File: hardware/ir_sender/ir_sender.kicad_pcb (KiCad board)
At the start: 2 copper layers, 3 parts, among them J1 Conn_01x05

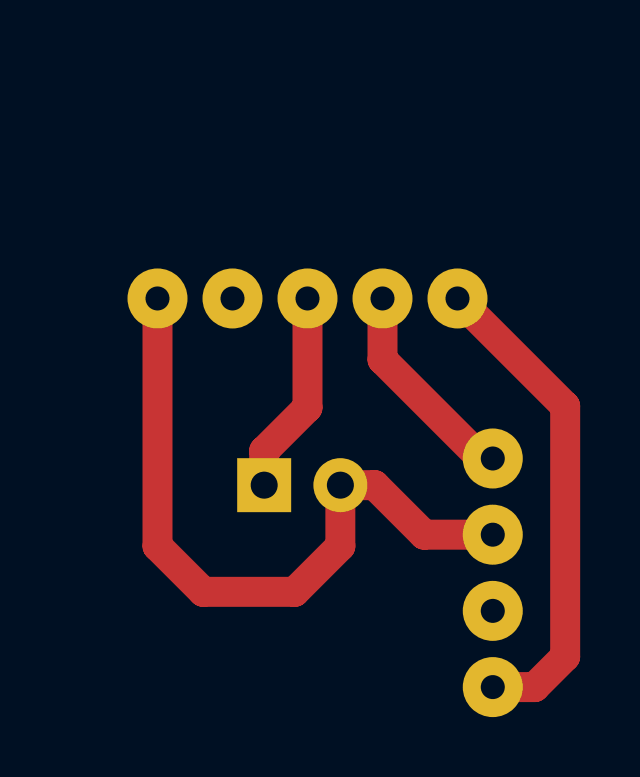
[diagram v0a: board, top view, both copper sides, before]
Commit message: New ir sender board
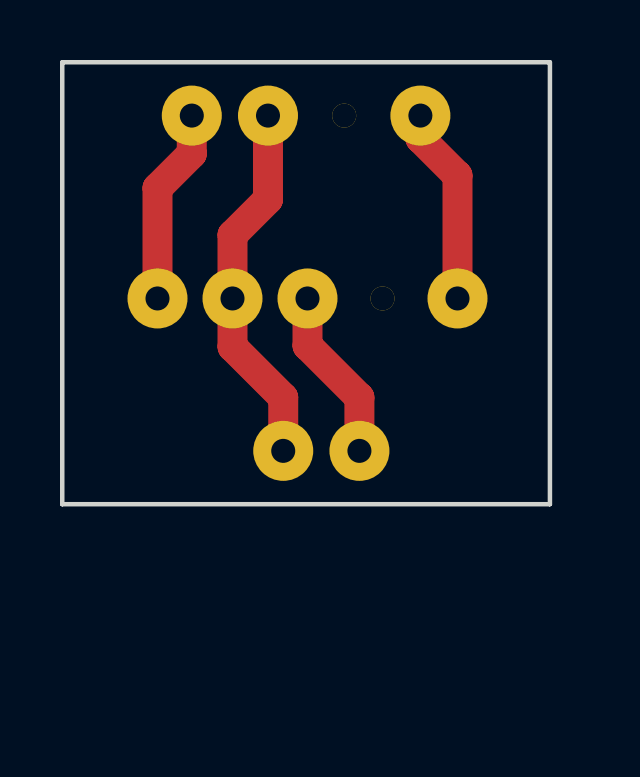
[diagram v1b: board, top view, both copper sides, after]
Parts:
- D1: footprint Pin_Headers:Pin_Header_Straight_1x04_Pitch2.54mm -> Socket_Strips:Socket_Strip_Straight_1x04_Pitch2.54mm
- D2: footprint LED_THT:LED_D5.0mm -> Socket_Strips:Socket_Strip_Straight_1x02_Pitch2.54mm
- moved D1 19.2 mm to (157.0, 116.3), turned to 90 degrees
- moved D2 3.37 mm to (154.9, 127.5), turned to 90 degrees
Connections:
- J1 pad 1: +5V -> /DinLed
- J1 pad 2: GND -> +5V
- J1 pad 4: /DinLed -> GND
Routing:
- net +5V: track 23.7 -> 12.4 mm
- net /DoutLed: track 16.3 -> 6.61 mm
- net Net-(D2-Pad1): track 6.82 -> 5.80 mm
- added copper zone on F.Cu, net GND
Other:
- board outline added: 16.3 x 14.7 mm
